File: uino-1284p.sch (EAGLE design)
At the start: 59 parts, among them J1 POWER, J2 POWER_JACKPTH, J3 M03X2, J4 POWER_SELECT, J5 M03X2, J6 IO, J7 ANALOG, J8 IOL, J9 IOH, U1 LD117AS50TR, U2 ATMEGA1284AU, U3 ATMEGA8U2AU, X1 16MHz, X2 16MHz

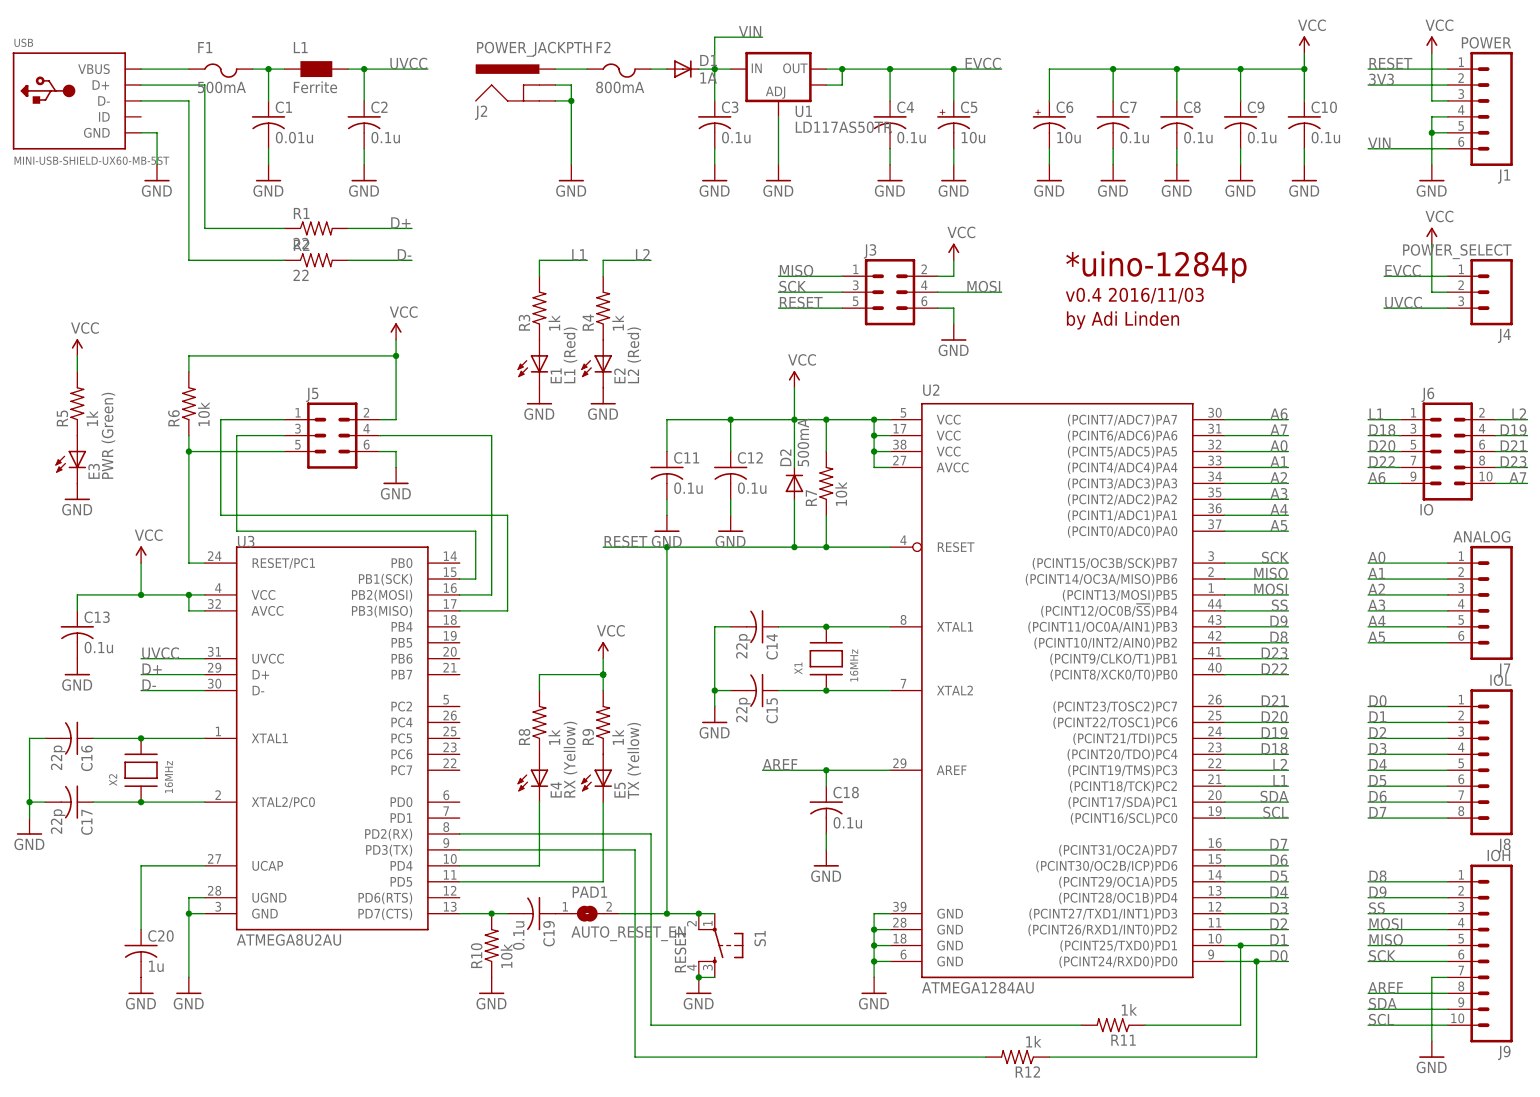
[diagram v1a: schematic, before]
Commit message: Changed to micro USB. Moved USB ICSP header.
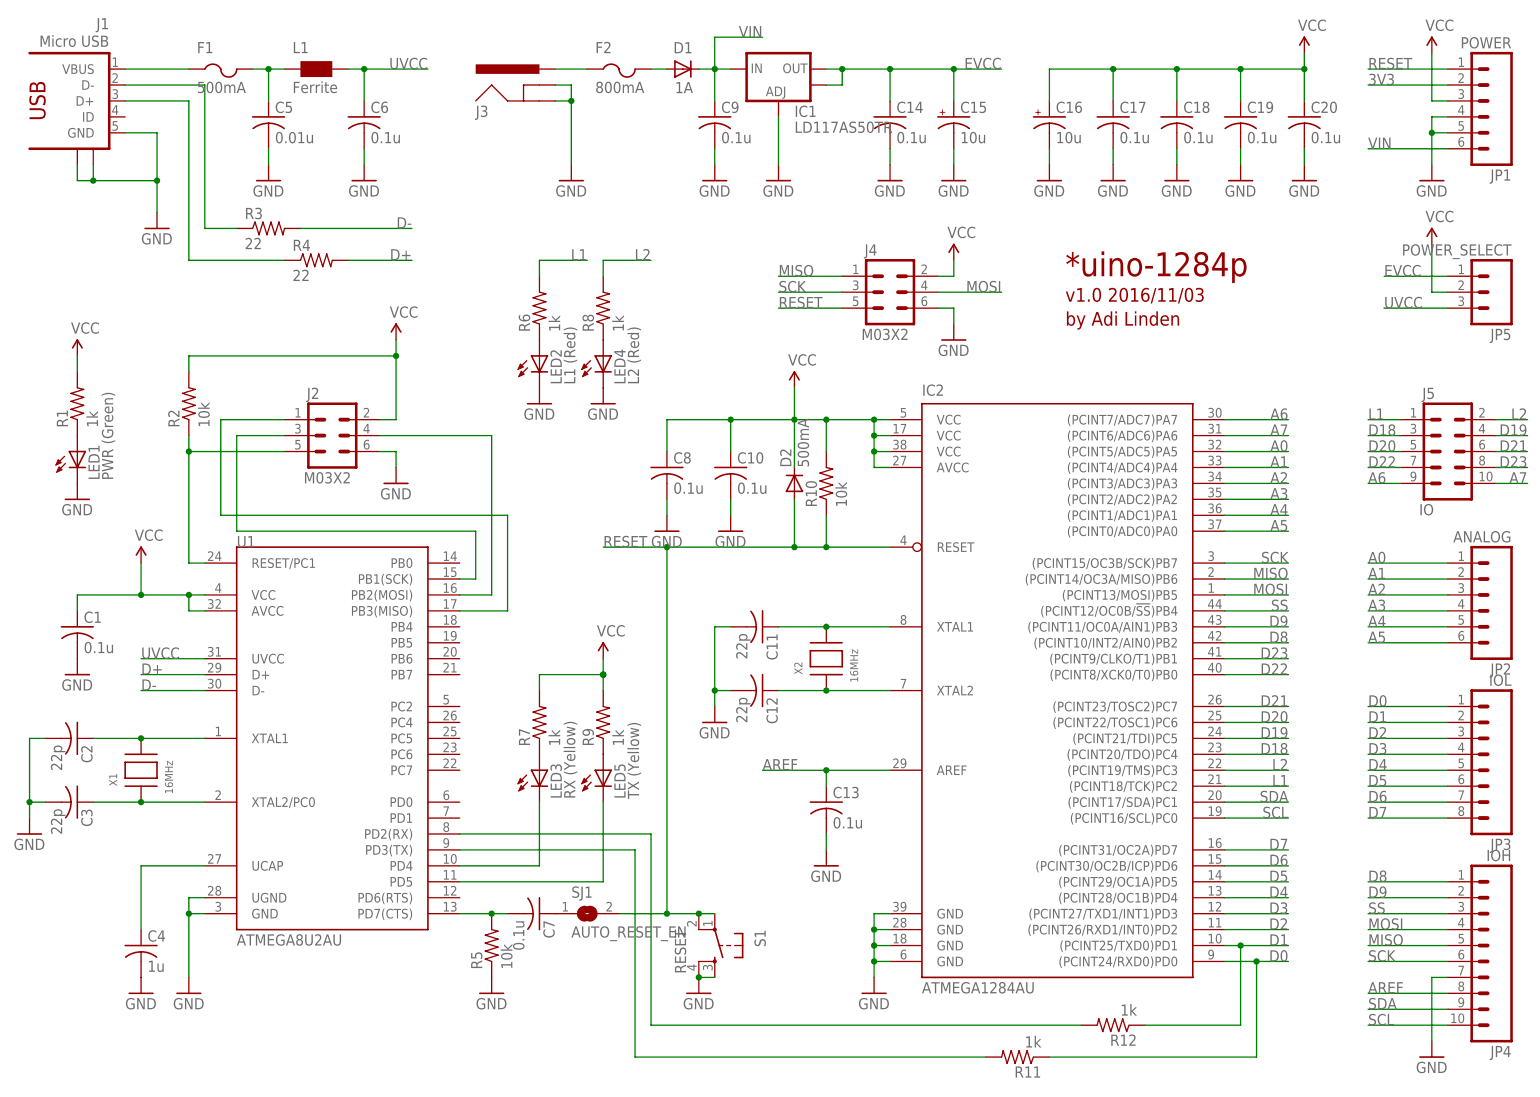
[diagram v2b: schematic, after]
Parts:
- removed J6: IO, adilinden:M05X2
- removed U3: ATMEGA8U2AU, SparkFun:ATMEGA8U2AU
- removed USB: MINI-USB-SHIELD-UX60-MB-5ST, adafruit:USBMINIB
- added IC1: LD117AS50TR, adilinden:V_REG_LM1117SOT223
- added JP1: POWER, SparkFun:M06SIP
- added JP5: POWER_SELECT, SparkFun:M03PTH
- C1: value 0.01u -> 0.1u
- C11, C12, C2, C3: value 0.1u -> 22p
- C14, C17: value 22p -> 0.1u
- C15, C16: value 22p -> 10u; device rcl:C-USC0805 -> rcl:CPOL-USCT3216
- C20: value 1u -> 0.1u
- C4: value 0.1u -> 1u
- C5: value 10u -> 0.01u; device rcl:CPOL-USCT3216 -> rcl:C-USC0805
- C6: value 10u -> 0.1u; device rcl:CPOL-USCT3216 -> rcl:C-USC0805
- J1: value POWER -> Micro USB; device SparkFun:M06SIP -> adi-misc:USB_MICRO_B_2.0-TH
- J2: value POWER_JACKPTH -> M03X2; device SparkFun:POWER_JACKPTH -> adi-misc:M03X2
- J3: value M03X2 -> POWER_JACKPTH; device adilinden:M03X2 -> SparkFun:POWER_JACKPTH
- J4: value POWER_SELECT -> M03X2; device SparkFun:M03PTH -> adi-misc:M03X2
- J5: value M03X2 -> IO; device adilinden:M03X2 -> adilinden:M05X2
- R1: value 22 -> 1k
- R2: value 22 -> 10k
- R3, R4: value 1k -> 22
- R5: value 1k -> 10k
- R6, R7: value 10k -> 1k
- U1: value LD117AS50TR -> ATMEGA8U2AU; device adilinden:V_REG_LM1117SOT223 -> SparkFun:ATMEGA8U2AU
- renumbered E1 to LED2, E2 to LED4, E3 to LED1, E4 to LED3, E5 to LED5, J7 to JP2, J8 to JP3, J9 to JP4, PAD1 to SJ1, U2 to IC2
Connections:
- net 3V3: now also JP1.2; no longer J1.2
- net A6: now also J5.9; no longer J6.9
- net A7: now also J5.10; no longer J6.10
- net AREF: now also C13.1; no longer C18.1
- net D+: now also R4.2, U1.D+; no longer R1.2, U3.D+
- net D-: now also R3.2, U1.D-; no longer R2.2, U3.D-
- net D0: now also R11.1; no longer R12.1
- net D1: now also R12.1; no longer R11.1
- net D18: now also J5.3; no longer J6.3
- net D19: now also J5.4; no longer J6.4
- net D20: now also J5.5; no longer J6.5
- net D21: now also J5.6; no longer J6.6
- net D22: now also J5.7; no longer J6.7
- net D23: now also J5.8; no longer J6.8
- net EVCC: now also C14.1, C15.+, IC1.OUT, IC1.OUT@1, JP5.1; no longer C4.1, C5.+, J4.1, U1.OUT, U1.OUT@1
- net GND: now also C15.-, C16.-, C19.2, C5.2, C6.2, IC1.ADJ, J1.GND, J1.S1, J1.S2, J2.6, J3.GND, J3.GNDBREAK, J4.6, JP1.4, JP1.5, R5.1, U1.GND, U1.UGND; no longer C15.2, C16.2, C5.-, C6.-, C7.2, J1.4, J1.5, J2.GND, J2.GNDBREAK, J3.6, J5.6, R10.1, U1.ADJ, U3.GND, U3.UGND, USB.GND
- net L1: now also J5.1, R6.2; no longer J6.1, R3.2
- net L2: now also J5.2, R8.2; no longer J6.2, R4.2
- net MISO: now also J4.1; no longer J3.1
- net MOSI: now also J4.4; no longer J3.4
- net N$10: now also C4.1, U1.UCAP; no longer C20.1, U3.UCAP
- net N$11: now also R6.1; no longer R3.1
- net N$12: now also R8.1; no longer R4.1
- net N$13: now also J2.1, U1.PB3(MISO); no longer J5.1, U3.PB3(MISO)
- net N$14: now also J2.3, U1.PB1(SCK); no longer J5.3, U3.PB1(SCK)
- net N$15: now also J2.5, R2.1, U1.RESET/PC1; no longer J5.5, R6.1, U3.RESET/PC1
- net N$16: now also J2.4, U1.PB2(MOSI); no longer J5.4, U3.PB2(MOSI)
- net N$2: now also C5.1; no longer C1.1
- net N$23: now also C11.1, X2.P$2; no longer C14.1, X1.P$2
- net N$24: now also C12.1, X2.P$1; no longer C15.1, X1.P$1
- net N$25: now also J3.PWR; no longer J2.PWR
- net N$26: now also R7.1; no longer R8.1
- net N$29: now also U1.PD4; no longer U3.PD4
- net N$3: now also C7.1; no longer C19.1
- net N$30: now also U1.PD5; no longer U3.PD5
- net N$31: now also C7.2, R5.2, U1.PD7(CTS); no longer C19.2, R10.2, U3.PD7(CTS)
- net N$34: now also R1.1; no longer R5.1
- net N$4: now also J1.D-, R3.1; no longer R2.1, USB.D-
- net N$5: now also J1.D+, R4.1; no longer R1.1, USB.D+
- net N$6: now also R11.2, U1.PD3(TX); no longer R12.2, U3.PD3(TX)
- net N$7: now also R12.2, U1.PD2(RX); no longer R11.2, U3.PD2(RX)
- net N$8: now also C2.1, U1.XTAL1, X1.P$2; no longer C16.1, U3.XTAL1, X2.P$2
- net N$9: now also C3.1, U1.XTAL2/PC0, X1.P$1; no longer C17.1, U3.XTAL2/PC0, X2.P$1
- net RESET: now also J4.5, JP1.1, R10.1; no longer J1.1, J3.5, R7.1
- net SCK: now also J4.3; no longer J3.3
- net UVCC: now also C6.1, JP5.3, U1.UVCC; no longer C2.1, J4.3, U3.UVCC
- net VBUS: now also J1.VBUS; no longer USB.VBUS
- net VCC: now also C1.1, C16.+, C17.1, C18.1, C19.1, C20.1, J2.2, JP1.3, JP5.2, R1.2, R10.2, R2.2, U1.AVCC, U1.VCC; no longer C11.1, C12.1, C13.1, C6.+, C7.1, C9.1, J1.3, J3.2, J5.2, R5.2, R6.2, R8.2, U3.AVCC, U3.VCC
- net VIN: now also C9.1, IC1.IN, JP1.6; no longer C3.1, J1.6, U1.IN
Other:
- note added: "v1.0 2016/11/03"
- note removed: "v0.4 2016/11/03"
- moved on the sheet: C1, C10, C11, C12, C13, C14, C17, C18, C19, C2, C20, C3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

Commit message: Made prefix for IC consistent.
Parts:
- removed IC2: ATMEGA1284AU, adilinden:ATMEGA1284P-AU
- added U2: ATMEGA1284AU, adi-atmega:ATMEGA1284P-AU
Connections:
- net A0: now also U2.(PCINT5/ADC5)PA5; no longer IC2.(PCINT5/ADC5)PA5
- net A1: now also U2.(PCINT4/ADC4)PA4; no longer IC2.(PCINT4/ADC4)PA4
- net A2: now also U2.(PCINT3/ADC3)PA3; no longer IC2.(PCINT3/ADC3)PA3
- net A3: now also U2.(PCINT2/ADC2)PA2; no longer IC2.(PCINT2/ADC2)PA2
- net A4: now also U2.(PCINT1/ADC1)PA1; no longer IC2.(PCINT1/ADC1)PA1
- net A5: now also U2.(PCINT0/ADC0)PA0; no longer IC2.(PCINT0/ADC0)PA0
- net A6: now also U2.(PCINT7/ADC7)PA7; no longer IC2.(PCINT7/ADC7)PA7
- net A7: now also U2.(PCINT6/ADC6)PA6; no longer IC2.(PCINT6/ADC6)PA6
- net AREF: now also U2.AREF; no longer IC2.AREF
- net D0: now also U2.(PCINT24/RXD0)PD0; no longer IC2.(PCINT24/RXD0)PD0
- net D1: now also U2.(PCINT25/TXD0)PD1; no longer IC2.(PCINT25/TXD0)PD1
- net D18: now also U2.(PCINT20/TDO)PC4; no longer IC2.(PCINT20/TDO)PC4
- net D19: now also U2.(PCINT21/TDI)PC5; no longer IC2.(PCINT21/TDI)PC5
- net D2: now also U2.(PCINT26/RXD1/INT0)PD2; no longer IC2.(PCINT26/RXD1/INT0)PD2
- net D20: now also U2.(PCINT22/TOSC1)PC6; no longer IC2.(PCINT22/TOSC1)PC6
- net D21: now also U2.(PCINT23/TOSC2)PC7; no longer IC2.(PCINT23/TOSC2)PC7
- net D22: now also U2.(PCINT8/XCK0/T0)PB0; no longer IC2.(PCINT8/XCK0/T0)PB0
- net D23: now also U2.(PCINT9/CLKO/T1)PB1; no longer IC2.(PCINT9/CLKO/T1)PB1
- net D3: now also U2.(PCINT27/TXD1/INT1)PD3; no longer IC2.(PCINT27/TXD1/INT1)PD3
- net D4: now also U2.(PCINT28/OC1B)PD4; no longer IC2.(PCINT28/OC1B)PD4
- net D5: now also U2.(PCINT29/OC1A)PD5; no longer IC2.(PCINT29/OC1A)PD5
- net D6: now also U2.(PCINT30/OC2B/ICP)PD6; no longer IC2.(PCINT30/OC2B/ICP)PD6
- net D7: now also U2.(PCINT31/OC2A)PD7; no longer IC2.(PCINT31/OC2A)PD7
- net D8: now also U2.(PCINT10/INT2/AIN0)PB2; no longer IC2.(PCINT10/INT2/AIN0)PB2
- net D9: now also U2.(PCINT11/OC0A/AIN1)PB3; no longer IC2.(PCINT11/OC0A/AIN1)PB3
- net GND: now also U2.GND, U2.GND@1, U2.GND@2, U2.GND@3; no longer IC2.GND, IC2.GND@1, IC2.GND@2, IC2.GND@3
- net L1: now also U2.(PCINT18/TCK)PC2; no longer IC2.(PCINT18/TCK)PC2
- net L2: now also U2.(PCINT19/TMS)PC3; no longer IC2.(PCINT19/TMS)PC3
- net MISO: now also U2.(PCINT14/OC3A/MISO)PB6; no longer IC2.(PCINT14/OC3A/MISO)PB6
- net MOSI: now also U2.(PCINT13/MOSI)PB5; no longer IC2.(PCINT13/MOSI)PB5
- net N$23: now also U2.XTAL1; no longer IC2.XTAL1
- net N$24: now also U2.XTAL2; no longer IC2.XTAL2
- net RESET: now also U2.RESET; no longer IC2.RESET
- net SCK: now also U2.(PCINT15/OC3B/SCK)PB7; no longer IC2.(PCINT15/OC3B/SCK)PB7
- net SCL: now also U2.(PCINT16/SCL)PC0; no longer IC2.(PCINT16/SCL)PC0
- net SDA: now also U2.(PCINT17/SDA)PC1; no longer IC2.(PCINT17/SDA)PC1
- net SS: now also U2.(PCINT12/OC0B/!SS!)PB4; no longer IC2.(PCINT12/OC0B/!SS!)PB4
- net VCC: now also U2.AVCC, U2.VCC, U2.VCC@1, U2.VCC@2; no longer IC2.AVCC, IC2.VCC, IC2.VCC@1, IC2.VCC@2

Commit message: Moved VCC lines. Fixed more naming.
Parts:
- removed IC1: LD117AS50TR, adilinden:V_REG_LM1117SOT223
- added U3: ATMEGA1284AU, adi-atmega:ATMEGA1284P-AU
- F1: value 500mA -> 350mA
- F2: value 800mA -> 750mA
- U2: value ATMEGA1284AU -> LD117AS50TR; device adi-atmega:ATMEGA1284P-AU -> adi-misc:V_REG_LM1117SOT223
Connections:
- net A0: now also U3.(PCINT5/ADC5)PA5; no longer U2.(PCINT5/ADC5)PA5
- net A1: now also U3.(PCINT4/ADC4)PA4; no longer U2.(PCINT4/ADC4)PA4
- net A2: now also U3.(PCINT3/ADC3)PA3; no longer U2.(PCINT3/ADC3)PA3
- net A3: now also U3.(PCINT2/ADC2)PA2; no longer U2.(PCINT2/ADC2)PA2
- net A4: now also U3.(PCINT1/ADC1)PA1; no longer U2.(PCINT1/ADC1)PA1
- net A5: now also U3.(PCINT0/ADC0)PA0; no longer U2.(PCINT0/ADC0)PA0
- net A6: now also U3.(PCINT7/ADC7)PA7; no longer U2.(PCINT7/ADC7)PA7
- net A7: now also U3.(PCINT6/ADC6)PA6; no longer U2.(PCINT6/ADC6)PA6
- net AREF: now also U3.AREF; no longer U2.AREF
- net D0: now also U3.(PCINT24/RXD0)PD0; no longer U2.(PCINT24/RXD0)PD0
- net D1: now also U3.(PCINT25/TXD0)PD1; no longer U2.(PCINT25/TXD0)PD1
- net D18: now also U3.(PCINT20/TDO)PC4; no longer U2.(PCINT20/TDO)PC4
- net D19: now also U3.(PCINT21/TDI)PC5; no longer U2.(PCINT21/TDI)PC5
- net D2: now also U3.(PCINT26/RXD1/INT0)PD2; no longer U2.(PCINT26/RXD1/INT0)PD2
- net D20: now also U3.(PCINT22/TOSC1)PC6; no longer U2.(PCINT22/TOSC1)PC6
- net D21: now also U3.(PCINT23/TOSC2)PC7; no longer U2.(PCINT23/TOSC2)PC7
- net D22: now also U3.(PCINT8/XCK0/T0)PB0; no longer U2.(PCINT8/XCK0/T0)PB0
- net D23: now also U3.(PCINT9/CLKO/T1)PB1; no longer U2.(PCINT9/CLKO/T1)PB1
- net D3: now also U3.(PCINT27/TXD1/INT1)PD3; no longer U2.(PCINT27/TXD1/INT1)PD3
- net D4: now also U3.(PCINT28/OC1B)PD4; no longer U2.(PCINT28/OC1B)PD4
- net D5: now also U3.(PCINT29/OC1A)PD5; no longer U2.(PCINT29/OC1A)PD5
- net D6: now also U3.(PCINT30/OC2B/ICP)PD6; no longer U2.(PCINT30/OC2B/ICP)PD6
- net D7: now also U3.(PCINT31/OC2A)PD7; no longer U2.(PCINT31/OC2A)PD7
- net D8: now also U3.(PCINT10/INT2/AIN0)PB2; no longer U2.(PCINT10/INT2/AIN0)PB2
- net D9: now also U3.(PCINT11/OC0A/AIN1)PB3; no longer U2.(PCINT11/OC0A/AIN1)PB3
- net EVCC: now also U2.OUT, U2.OUT@1; no longer IC1.OUT, IC1.OUT@1
- net GND: now also U2.ADJ, U3.GND, U3.GND@1, U3.GND@2, U3.GND@3; no longer IC1.ADJ, U2.GND, U2.GND@1, U2.GND@2, U2.GND@3
- net L1: now also U3.(PCINT18/TCK)PC2; no longer U2.(PCINT18/TCK)PC2
- net L2: now also U3.(PCINT19/TMS)PC3; no longer U2.(PCINT19/TMS)PC3
- net MISO: now also U3.(PCINT14/OC3A/MISO)PB6; no longer U2.(PCINT14/OC3A/MISO)PB6
- net MOSI: now also U3.(PCINT13/MOSI)PB5; no longer U2.(PCINT13/MOSI)PB5
- net N$23: now also U3.XTAL1; no longer U2.XTAL1
- net N$24: now also U3.XTAL2; no longer U2.XTAL2
- net RESET: now also U3.RESET; no longer U2.RESET
- net SCK: now also U3.(PCINT15/OC3B/SCK)PB7; no longer U2.(PCINT15/OC3B/SCK)PB7
- net SCL: now also U3.(PCINT16/SCL)PC0; no longer U2.(PCINT16/SCL)PC0
- net SDA: now also U3.(PCINT17/SDA)PC1; no longer U2.(PCINT17/SDA)PC1
- net SS: now also U3.(PCINT12/OC0B/!SS!)PB4; no longer U2.(PCINT12/OC0B/!SS!)PB4
- net VCC: now also U3.AVCC, U3.VCC, U3.VCC@1, U3.VCC@2; no longer U2.AVCC, U2.VCC, U2.VCC@1, U2.VCC@2
- net VIN: now also U2.IN; no longer IC1.IN
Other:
- note added: "v1.1 2016/11/05"
- note removed: "v1.0 2016/11/03"
